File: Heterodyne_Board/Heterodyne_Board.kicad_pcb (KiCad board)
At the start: 2 copper layers, 57.4 x 69.5 mm, 57 parts, among them J1 AVR-ISP-6, J2 Speaker, J3 SWITCH, J4 LED, J6 AudioJack2_Ground_Switch, J7 Barrel_Jack, SW1 SW_SPST, SW2 SW_SPST, U1 ATtiny85-20P, U2 TLV9054xD, U3 AP2112K-3.3, U4 LM386, U5 W25X40CLSN, U6 TS5A3159DCK

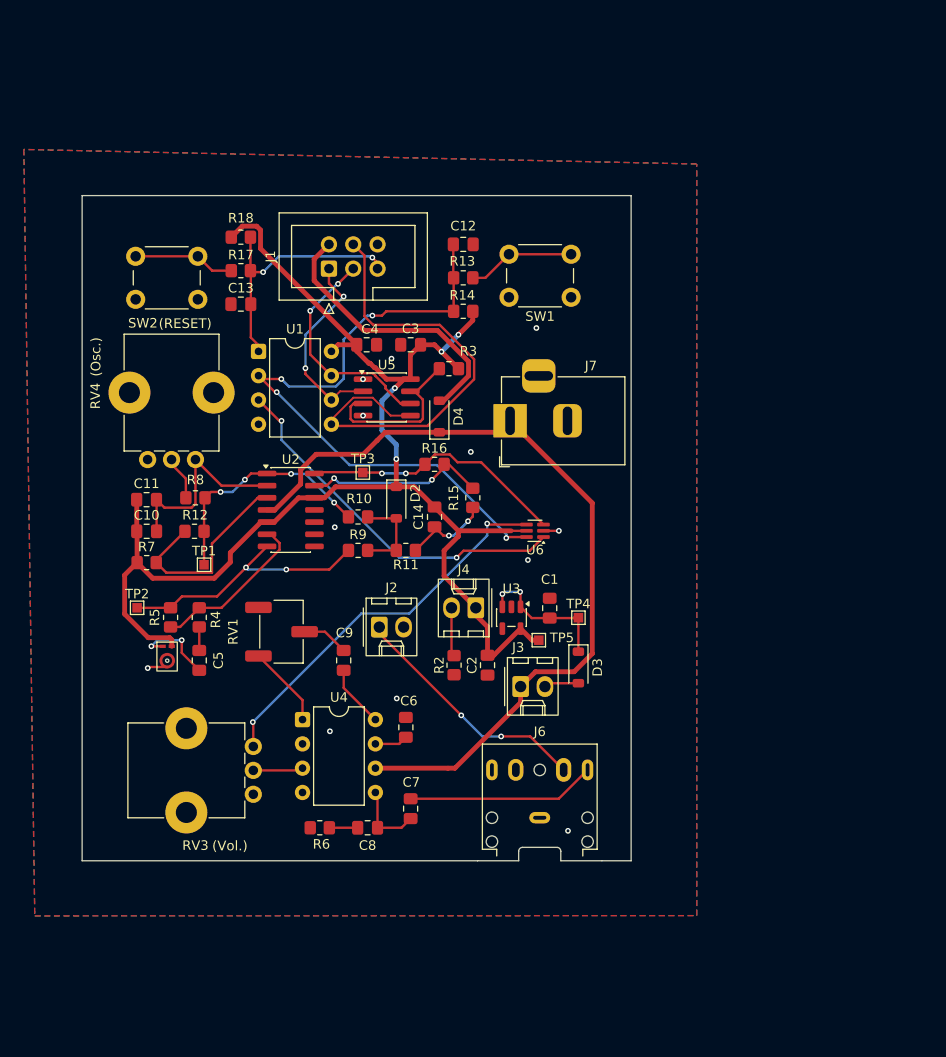
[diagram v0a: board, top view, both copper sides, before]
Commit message: Board round 2 complete, GBRs sent
Also removed some of the automatic backups cuz they weren't necessary. Made discrete footprint for microphone
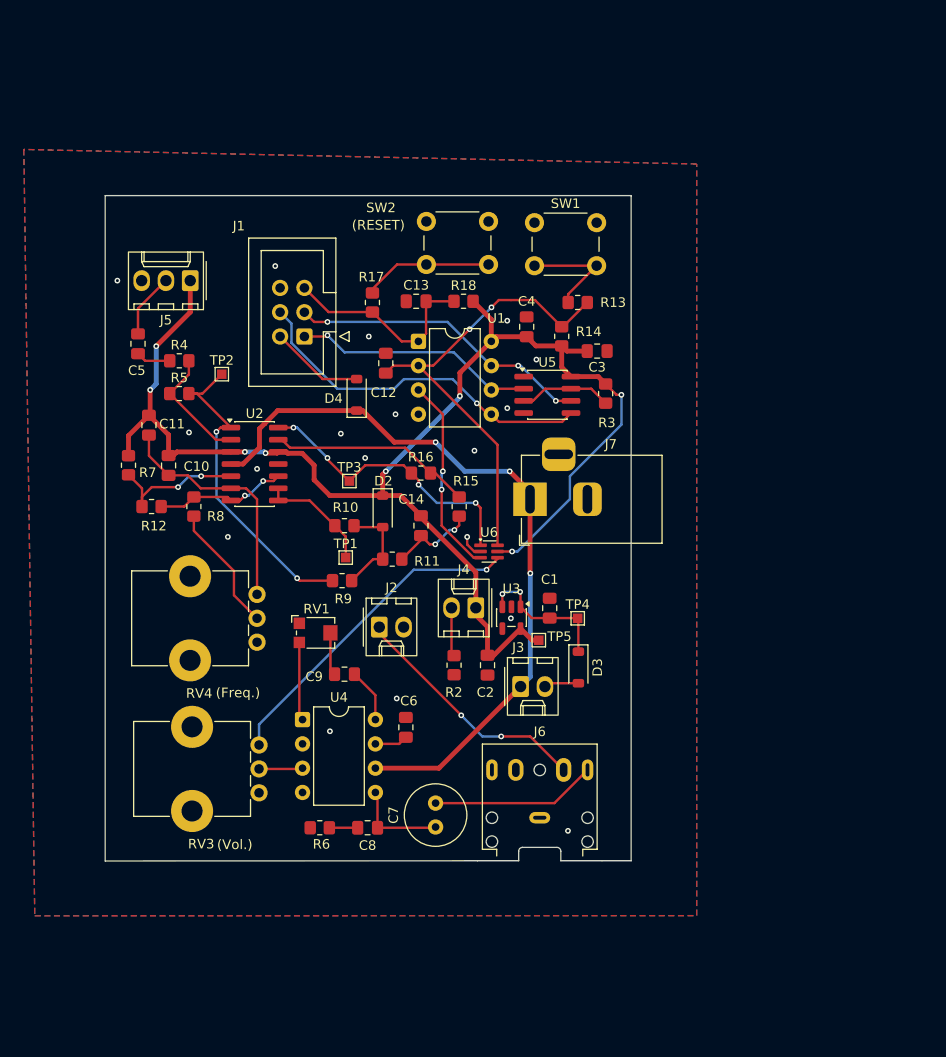
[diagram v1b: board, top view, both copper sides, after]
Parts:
- removed MK1: Microphone, Sensor_Audio:Knowles_LGA-5_3.5x2.65mm
- added J5: Microphone, Connector_Molex:Molex_KK-254_AE-6410-03A_1x03_P2.54mm_Vertical, F.Cu at (148.0, 69.3)
- C7: footprint Capacitor_SMD:C_0805_2012Metric_Pad1.18x1.45mm_HandSolder -> Capacitor_THT:C_Radial_D6.3mm_H11.0mm_P2.50mm
- RV1: footprint Potentiometer_SMD:Potentiometer_Bourns_3269W_Vertical -> Potentiometer_SMD:Potentiometer_Bourns_TC33X_Vertical
- SW1, SW2: footprint Button_Switch_THT:SW_PUSH_6mm_H13mm -> Button_Switch_THT:SW_PUSH_6mm_H5mm
- moved C5 33.7 mm to (142.5, 75.9), turned to -90 degrees
- moved R4 26.9 mm to (146.8, 77.7), turned to 0 degrees
- moved TP2 26.0 mm to (151.3, 79.1)
- moved SW2 25.2 mm to (172.6, 63.2), turned to 0 degrees
- moved R18 24.2 mm to (176.5, 71.5), turned to 0 degrees
- moved R5 23.4 mm to (146.8, 81.2), turned to 0 degrees
- moved C3 19.5 mm to (190.5, 76.7), turned to 180 degrees
- moved C13 18.3 mm to (171.6, 71.5)
- moved C4 16.8 mm to (183.1, 74.2), turned to -90 degrees
- moved U5 16.8 mm to (185.3, 81.3)
- moved U1 16.8 mm to (171.8, 75.7)
- moved R3 16.6 mm to (191.4, 81.2), turned to -90 degrees
- moved RV4 15.5 mm to (154.9, 102.1), turned to 180 degrees
- moved C12 14.8 mm to (168.4, 78.0), turned to -90 degrees
- moved TP1 14.8 mm to (164.2, 98.3)
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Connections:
- C10 pad 2: Net-(U2A--) -> Net-(U2B--)
- C11 pad 2: Net-(U2A--) -> Net-(U2B--)
- R12 pad 1: Net-(U2A-+) -> Net-(U2B-+)
- R12 pad 2: /Osci_out -> Net-(U2C-+)
- R16 pad 2: /Mixer_Out -> /Mixer_out
- R4 pad 2: Net-(U2B--) -> Net-(U2A--)
- R5 pad 1: Net-(U2B--) -> Net-(U2A--)
- R7 pad 2: Net-(U2A-+) -> Net-(U2B-+)
- R8 pad 1: /Osci_out -> Net-(U2C-+)
- RV4 pad 1: Net-(U2A--) -> Net-(U2B--)
- TP3 pad 1: /Mixer_Out -> /Mixer_out
- U1 pad 3: /MCU_Out -> /MCU_out
- U2 pad 1: /Osci_out -> /Mic_out
- U2 pad 10: unconnected-(U2C-+-Pad10) -> Net-(U2C-+)
- U2 pad 14: /Mixer_Out -> /Mixer_out
- U2 pad 3: Net-(U2A-+) -> +3V3
- U2 pad 5: +3V3 -> Net-(U2B-+)
- U2 pad 7: /Mic_out -> Net-(U2C-+)
- U2 pad 8: unconnected-(U2-Pad8) -> /Osci_out
- U2 pad 9: unconnected-(U2C---Pad9) -> /Osci_out
- U6 pad 1: /MCU_Out -> /Mixer_out
- U6 pad 3: /Mixer_Out -> /MCU_out
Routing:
- net /MCU_Out: track 38.7 -> 0.00 mm, vias 2 -> 0
- net /Mixer_out: track 0.00 -> 30.3 mm, vias 0 -> 4
- net /Mixer_Out: track 27.9 -> 0.00 mm, vias 2 -> 0
- net Net-(U2A-+): track 21.6 -> 0.00 mm
- net /MCU_out: track 0.00 -> 20.8 mm, vias 0 -> 2
- net /Audio_EN: track 69.2 -> 48.6 mm, vias 4 -> 2
- net Net-(D4-A): track 29.7 -> 9.84 mm
- net Net-(U2B-+): track 0.00 -> 15.1 mm, vias 0 -> 2
- net Net-(U2C-+): track 0.00 -> 13.9 mm, vias 0 -> 2
- net /MOSI: track 50.9 -> 37.6 mm, vias 0 -> 1
- net /Osci_out: track 25.0 -> 12.0 mm, vias 4 -> 0
- net +6V: track 86.7 -> 77.8 mm, vias 0 -> 3
- net Net-(R8-Pad2): track 4.62 -> 13.4 mm
- net Net-(U5-~{HOLD}): track 18.2 -> 9.72 mm
- net Net-(U2A--): track 21.1 -> 12.7 mm
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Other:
- board size 57.4 x 69.5 mm -> 55 x 69.6 mm
- board text added: "(Freq.)"
- board text removed: "(Osc.)"

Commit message: Updated PCB
Mounting holes, second ISP header, wider board. Total dimensions about 70x70mm now.
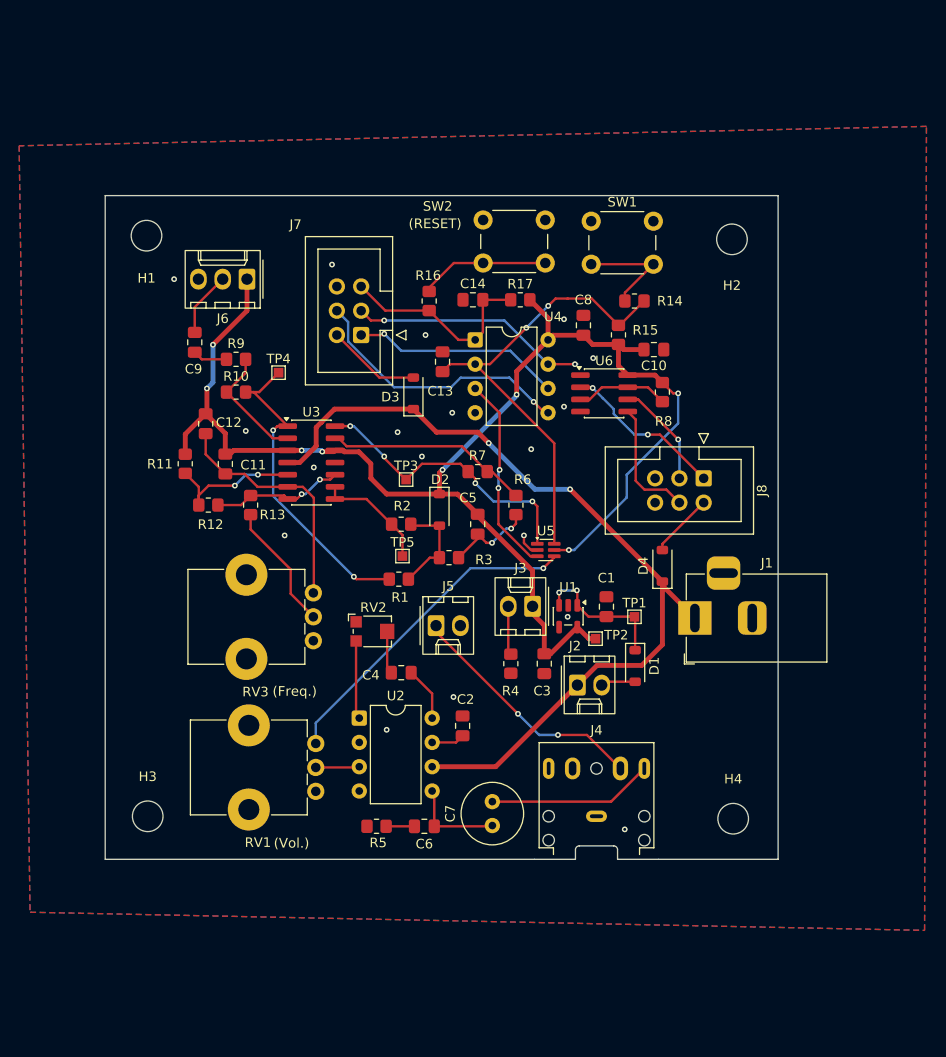
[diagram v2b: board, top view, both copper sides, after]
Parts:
- removed RV4: R_Potentiometer, Potentiometer_THT:Potentiometer_Bourns_PTV09A-1_Single_Vertical
- added D4: Schottky, Diode_SMD:D_SOD-123, F.Cu at (197.3, 99.2)
- added H1: MountingHole, MountingHole:MountingHole_3.2mm_M3, F.Cu at (143.4, 64.6)
- added H2: MountingHole, MountingHole:MountingHole_3.2mm_M3, F.Cu at (204.6, 65.0)
- added H3: MountingHole, MountingHole:MountingHole_3.2mm_M3, F.Cu at (143.5, 125.3)
- added H4: MountingHole, MountingHole:MountingHole_3.2mm_M3, F.Cu at (204.7, 125.6)
- added J8: AVR-ISP-6, Connector_IDC:IDC-Header_2x03_P2.54mm_Vertical, F.Cu at (201.6, 90.0)
- added RV3: R_Potentiometer, Potentiometer_THT:Potentiometer_Bourns_PTV09A-1_Single_Vertical, F.Cu at (160.8, 102.0)
- D1: renamed from D3; value MBR0520 -> Schottky
- D2: value MBR0520 -> Schottky
- D3: renamed from D4; value MBR0520 -> Schottky
- moved J1 21.2 mm to (200.7, 104.6)
- moved C11 5.94 mm to (151.6, 88.5)
- moved C13 5.94 mm to (174.3, 77.8)
- moved C8 5.94 mm to (189.1, 74.0)
- moved C1 5.94 mm to (191.5, 103.4)
- moved C10 5.94 mm to (196.4, 76.6)
- moved C12 5.94 mm to (149.6, 84.3)
- moved C14 5.94 mm to (177.5, 71.3)
- moved C2 5.94 mm to (176.4, 115.9)
- moved C3 5.94 mm to (185.0, 109.4)
- moved C4 5.94 mm to (170.0, 110.3)
- moved C5 5.94 mm to (178.0, 94.8)
- moved C6 5.94 mm to (172.4, 126.4)
- moved C7 5.94 mm to (179.5, 126.3)
- moved C9 5.94 mm to (148.4, 75.8)
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- renumbered C3 to C10, C10 to C11, C11 to C12, C12 to C13, C13 to C14, C6 to C2, C2 to C3, C9 to C4, C14 to C5, C8 to C6, C4 to C8, C5 to C9, J7 to J1, J3 to J2, J4 to J3, J6 to J4, J2 to J5, J5 to J6, J1 to J7, R9 to R1, R5 to R10, R7 to R11, R8 to R13, R13 to R14, R14 to R15, R17 to R16, R18 to R17, R10 to R2, R11 to R3, R2 to R4, R6 to R5, R15 to R6, R16 to R7, R3 to R8, R4 to R9, RV3 to RV1, RV1 to RV2, TP4 to TP1, TP5 to TP2, TP2 to TP4, TP1 to TP5, U3 to U1, U4 to U2, U2 to U3, U1 to U4, U6 to U5, U5 to U6
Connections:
- net /RESET renamed /RESET_MCU
- J7 pad 1: /MISO -> /MISO_MCU
- J7 pad 3: /SCK -> /SCK_MCU
- J7 pad 4: /MOSI -> /MOSI_MCU
- U4 pad 5: /MOSI -> /MOSI_MCU
- U4 pad 6: /MISO -> /MISO_MCU
- U4 pad 7: /SCK -> /SCK_MCU
- U6 pad 2: /MISO -> /MISO_FLASH
- U6 pad 5: /MOSI -> /MOSI_FLASH
- U6 pad 6: /SCK -> /SCK_FLASH
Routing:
- net /MOSI: track 37.6 -> 0.00 mm, vias 1 -> 0
- net /SCK: track 31.7 -> 0.00 mm, vias 3 -> 0
- net /MOSI_MCU: track 0.00 -> 28.5 mm, vias 0 -> 1
- net /MISO: track 25.4 -> 0.00 mm, vias 1 -> 0
- net /SCK_MCU: track 0.00 -> 24.9 mm, vias 0 -> 2
- net /MISO_MCU: track 0.00 -> 22.1 mm, vias 0 -> 1
- net /MISO_FLASH: track 0.00 -> 17.1 mm, vias 0 -> 2
- net +6V: track 77.8 -> 91.3 mm, vias 3 -> 2
- net /MOSI_FLASH: track 0.00 -> 13.1 mm
- net /SCK_FLASH: track 0.00 -> 11.1 mm, vias 0 -> 1
- net Net-(D4-A): track 0.00 -> 6.74 mm
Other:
- board size 55 x 69.6 mm -> 70.4 x 69.4 mm

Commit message: Round 3 PCB upload
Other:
- board text added: "(FLASH)"
- board text added: "(MCU)"
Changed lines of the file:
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@@
 		(tags "Through hole vertical IDC box header THT 2x03 2.54mm double row")
 		(property "Reference" "J8"
-			(at 1.27 -6.1 90)
+			(at -6.322658 -3.718 180)
 			(layer "F.SilkS")
 			(effects
@@
 		(layer "F.SilkS")
 		(effects
+			(font
+				(size 1.016 1.016)
+				(thickness 0.1524)
+			)
+			(justify left bottom)
+		)
+	)
+	(gr_text "(FLASH)"
+		(at 202.565 85.852 0)
+		(layer "F.SilkS")
+		(effects
+			(font
+				(size 1.016 1.016)
+				(thickness 0.1524)
+			)
+			(justify left bottom)
+		)
+	)
+	(gr_text "(MCU)"
+		(at 160.528 64.008 0)
+		(layer "F.SilkS")
+		(effects

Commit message: FINAL BOARD REV
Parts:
- removed RV2: R_Potentiometer_Trim, Potentiometer_SMD:Potentiometer_Bourns_TC33X_Vertical
- removed RV3: R_Potentiometer, Potentiometer_THT:Potentiometer_Bourns_PTV09A-1_Single_Vertical
- added J10: Frequenciometer, Connector_Molex:Molex_KK-254_AE-6410-03A_1x03_P2.54mm_Vertical, F.Cu at (145.5, 111.5)
- added J11: Audio_EN, Connector_Molex:Molex_KK-254_AE-6410-02A_1x02_P2.54mm_Vertical, F.Cu at (198.0, 68.0)
- added J9: AVR-ISP-6, Connector_PinHeader_2.54mm:PinHeader_2x03_P2.54mm_Vertical, F.Cu at (171.7, 61.0)
- added R18: 470, Resistor_SMD:R_0805_2012Metric_Pad1.20x1.40mm_HandSolder, F.Cu at (167.0, 60.5)
- added R19: 1k, Resistor_SMD:R_0805_2012Metric_Pad1.20x1.40mm_HandSolder, F.Cu at (162.0, 60.5)
- added R20: 1k, Resistor_SMD:R_0805_2012Metric_Pad1.20x1.40mm_HandSolder, F.Cu at (191.0, 69.5)
- added R21: 1k, Resistor_SMD:R_0805_2012Metric_Pad1.20x1.40mm_HandSolder, F.Cu at (200.5, 109.0)
- added R22: 10k, Resistor_SMD:R_0805_2012Metric_Pad1.20x1.40mm_HandSolder, F.Cu at (183.5, 69.5)
- added R23: 10k, Resistor_SMD:R_0805_2012Metric_Pad1.20x1.40mm_HandSolder, F.Cu at (200.5, 112.0)
- added R24: 10k, Resistor_SMD:R_0805_2012Metric_Pad1.20x1.40mm_HandSolder, F.Cu at (185.5, 117.0)
- added R25: 1k, Resistor_SMD:R_0805_2012Metric_Pad1.20x1.40mm_HandSolder, F.Cu at (186.0, 120.5)
- J2: value SWITCH -> Volume; footprint Connector_Molex:Molex_KK-254_AE-6410-02A_1x02_P2.54mm_Vertical -> Connector_Molex:Molex_KK-254_AE-6410-03A_1x03_P2.54mm_Vertical
- J3: value LED -> SWITCH
- J4: value AudioJack2_Ground_Switch -> LED; footprint Connector_Audio:Jack_3.5mm_CUI_SJ1-3525N_Horizontal -> Connector_Molex:Molex_KK-254_AE-6410-02A_1x02_P2.54mm_Vertical
- J5: value Speaker -> AudioJack2_Ground_Switch; footprint Connector_Molex:Molex_KK-254_AE-6410-02A_1x02_P2.54mm_Vertical -> Connector_Audio:Jack_3.5mm_CUI_SJ1-3525N_Horizontal
- J6: value Microphone -> Speaker; footprint Connector_Molex:Molex_KK-254_AE-6410-03A_1x03_P2.54mm_Vertical -> Connector_Molex:Molex_KK-254_AE-6410-02A_1x02_P2.54mm_Vertical
- J7: value AVR-ISP-6 -> Microphone; footprint Connector_IDC:IDC-Header_2x03_P2.54mm_Vertical -> Connector_Molex:Molex_KK-254_AE-6410-03A_1x03_P2.54mm_Vertical
- R12, R16: value 1k -> 470
- R13: value 100 -> 1k
- R15: value 10k -> 100
- R17: value 10k -> 1k
- RV1: value R_Potentiometer -> R_Potentiometer_Trim; footprint Potentiometer_THT:Potentiometer_Bourns_PTV09A-1_Single_Vertical -> Potentiometer_SMD:Potentiometer_Bourns_TC33X_Vertical
- SW1, SW2: value SW_SPST -> SW_SPDT; footprint Button_Switch_THT:SW_PUSH_6mm_H5mm -> Button_Switch_THT:SW_Slide_SPDT_Straight_CK_OS102011MS2Q
- U6: value W25X40CLSN -> SST25VF080B; footprint Package_SO:SOIC-8_3.9x4.9mm_P1.27mm -> Package_DIP:DIP-8_W7.62mm
- moved J4 67.7 mm to (158.8, 65.5), turned to 180 degrees
- moved J6 66.7 mm to (195.3, 121.5)
- moved R14 60.4 mm to (152.5, 115.0)
- moved J1 59.0 mm to (148.0, 78.0), turned to 0 degrees
- moved D1 54.4 mm to (154.2, 73.0), turned to 90 degrees
- moved R15 49.0 mm to (160.0, 111.5), turned to 180 degrees
- moved TP1 48.0 mm to (154.3, 78.2), turned to 180 degrees
- moved C14 46.9 mm to (205.5, 109.0), turned to 180 degrees
- moved TP2 44.4 mm to (158.4, 75.9), turned to 180 degrees
- moved C1 41.9 mm to (157.2, 79.2), turned to -90 degrees
- moved C3 41.9 mm to (163.7, 73.3), turned to 90 degrees
- moved D4 41.9 mm to (178.0, 62.0)
- moved SW1 41.3 mm to (201.5, 102.8)
- moved R4 38.8 mm to (167.2, 73.3), turned to 90 degrees
- moved J5 37.1 mm to (194.0, 136.5)
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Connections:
- C13 pad 2: /Audio_EN -> /CANS
- C14 pad 2: /RESET_MCU -> /RESET
- C9 pad 1: Net-(J6-Pin_2) -> Net-(J7-Pin_2)
- D4 pad 1: +6V -> +3V3
- J2 pad 1: +6V -> GND
- J2 pad 2: Net-(D1-A) -> Net-(J2-Pin_2)
- J3 pad 1: +3V3 -> +6V
- J3 pad 2: Net-(J3-Pin_2) -> Net-(D1-A)
- J6 pad 1: +3V3 -> Net-(J6-Pin_1)
- J6 pad 2: Net-(J6-Pin_2) -> GND
- J7 pad 1: /MISO_MCU -> +3V3
- J7 pad 2: Net-(D3-A) -> Net-(J7-Pin_2)
- J7 pad 3: /SCK_MCU -> GND
- J8 pad 1: /MISO_FLASH -> /MISO
- J8 pad 2: Net-(D4-A) -> Net-(D3-A)
- J8 pad 3: /SCK_FLASH -> /SCK
- J8 pad 4: /MOSI_FLASH -> /MOSI
- J8 pad 5: unconnected-(J8-~{RST}-Pad5) -> /RESET
- R12 pad 1: Net-(U3B-+) -> Net-(J9-~{RST})
- R12 pad 2: Net-(U3C-+) -> /CANS
- R13 pad 1: Net-(U3C-+) -> GND
- R13 pad 2: Net-(R13-Pad2) -> /CANS
- R14 pad 1: Net-(SW1-B) -> Net-(U3B-+)
- R14 pad 2: /Audio_EN -> Net-(U3C-+)
- R15 pad 1: /Audio_EN -> Net-(U3C-+)
- R15 pad 2: +3V3 -> Net-(J10-Pin_2)
- R16 pad 1: Net-(SW2-B) -> Net-(J9-SCK)
- R16 pad 2: /RESET_MCU -> /SCK
- R17 pad 1: /RESET_MCU -> GND
- R17 pad 2: +3V3 -> /SCK
- R4 pad 1: Net-(J3-Pin_2) -> Net-(J4-Pin_2)
- RV1 pad 1: /Speaker_in -> unconnected-(RV1-Pad1)
- RV1 pad 2: Net-(U2-+) -> Net-(C4-Pad2)
- RV1 pad 3: GND -> Net-(RV1-Pad3)
- SW1 pad 1: GND -> Net-(SW1-A)
- SW1 pad 2: Net-(SW1-B) -> GND
- SW2 pad 1: GND -> Net-(J11-Pin_2)
- SW2 pad 2: Net-(SW2-B) -> GND
- U2 pad 1: Net-(RV2-Pad3) -> Net-(RV1-Pad3)
- U2 pad 3: Net-(U2-+) -> Net-(J2-Pin_2)
- U4 pad 1: /RESET_MCU -> /RESET
- U4 pad 2: /Audio_EN -> /CANS
- U4 pad 5: /MOSI_MCU -> /MOSI
- U4 pad 6: /MISO_MCU -> /MISO
- U4 pad 7: /SCK_MCU -> /SCK
- U5 pad 3: /MCU_out -> Net-(R24-Pad2)
- U5 pad 6: /Audio_EN -> /CANS
- U6 pad 1: GND -> /CANS
- U6 pad 2: /MISO_FLASH -> /MOSI
- U6 pad 5: /MOSI_FLASH -> /MISO
- U6 pad 6: /SCK_FLASH -> /SCK
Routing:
- net /MISO: track 0.00 -> 100.5 mm, vias 0 -> 4
- net /CANS: track 0.00 -> 85.5 mm, vias 0 -> 10
- net /MOSI: track 0.00 -> 83.8 mm, vias 0 -> 10
- net /SCK: track 0.00 -> 75.4 mm, vias 0 -> 8
- net /RESET: track 0.00 -> 53.6 mm, vias 0 -> 2
- net /Audio_EN: track 48.6 -> 0.00 mm, vias 2 -> 0
- net +3V3: track 150.1 -> 197.8 mm, vias 8 -> 2
- net +6V: track 91.3 -> 123.8 mm, vias 2 -> 0
- net /MOSI_MCU: track 28.5 -> 0.00 mm, vias 1 -> 0
- net Net-(J5-Pin_1): track 25.8 -> 0.00 mm, vias 2 -> 0
- net /SCK_MCU: track 24.9 -> 0.00 mm, vias 2 -> 0
- net Net-(J2-Pin_2): track 0.00 -> 24.4 mm, vias 0 -> 1
- net /MISO_MCU: track 22.1 -> 0.00 mm, vias 1 -> 0
- net /RESET_MCU: track 21.7 -> 0.00 mm
- net /Speaker_in: track 34.4 -> 13.4 mm, vias 1 -> 2
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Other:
- board size 70.4 x 69.4 mm -> 70.4 x 93 mm

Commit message: stared at bill pcb
it good
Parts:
- J10: value Frequenciometer -> Frequenciometer (1k)
- RV1: value R_Potentiometer_Trim -> 10k
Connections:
- C5 pad 1: Net-(C5-Pad1) -> +3V3
- C5 pad 2: +3V3 -> Net-(C5-Pad2)
- R3 pad 2: Net-(C5-Pad1) -> Net-(C5-Pad2)
- R6 pad 1: Net-(C5-Pad1) -> Net-(C5-Pad2)
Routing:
- net +3V3: track 197.8 -> 205.3 mm
- net Net-(C5-Pad1): track 7.52 -> 0.00 mm
- net /CANS: track 85.5 -> 84.9 mm, vias 10 -> 8
- net GND: vias 16 -> 21
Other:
- board size 70.4 x 93 mm -> 70.4 x 84 mm
- board text added: "(CANS)"
- board text added: "(Mic)"
